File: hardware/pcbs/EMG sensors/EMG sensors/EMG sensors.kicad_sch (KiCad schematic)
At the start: 28 parts, among them IC1 INA128, J1 Conn_01x04_Pin, J2 Conn_01x01_Pin, U6 OPA2188AIDR, U7 OPA188AIDR

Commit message: sEMG sensors v0.3
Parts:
- added R11: 1M, Resistor_SMD:R_0603_1608Metric_Pad0.98x0.95mm_HandSolder, symbol Device:R
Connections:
- net GND: now also R11.1; no longer J2.1 (Pin_1)
- new net Ref: J2.1 (Pin_1), R11.2
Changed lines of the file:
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@@
-	(wire
-		(pts
-			(xy 57.658 144.78) (xy 57.658 146.812)
-		)
-		(stroke
-			(width 0)
-			(type default)
-		)
-	)
 	(wire
 		(pts
@@
 	(wire
 		(pts
+			(xy 57.658 144.78) (xy 57.658 147.574)
+		)
+		(stroke
+			(width 0)
+			(type default)
+		)
+	)
+	(wire
+		(pts
 			(xy 249.936 84.582) (xy 250.19 84.582)
 		)
@@
 	(wire
 		(pts
+			(xy 57.658 155.194) (xy 57.658 156.21)
+		)
+		(stroke
+			(width 0)
+			(type default)
+		)
+	)
+	(wire
+		(pts
 			(xy 202.692 84.582) (xy 212.344 84.582)
 		)
@@
 	(global_label "Ref"
 		(shape input)
-		(at 57.658 146.812 270)
+		(at 57.658 156.21 270)
 		(fields_autoplaced yes)
 		(effects
@@
 		)
 		(property "Intersheetrefs" "${INTERSHEET_REFS}"
-			(at 57.658 152.8815 90)
+			(at 57.658 162.2795 90)
 			(effects
 				(font
@@
 					(unit 1)
 				)
+			)
+		)
+	)
+	(symbol
+		(lib_id "Device:R")
+		(at 57.658 151.384 0)
+		(unit 1)
+		(exclude_from_sim no)
+		(in_bom yes)
+		(on_board yes)
+		(dnp no)
+		(fields_autoplaced yes)
+		(property "Reference" "R11"
+			(at 59.69 150.1139 0)
+			(effects
+				(font
+					(size 1.27 1.27)
+				)
+				(justify left)
+			)
+		)
+		(property "Value" "1M"
+			(at 59.69 152.6539 0)
+			(effects
+				(font
+					(size 1.27 1.27)
+				)
+				(justify left)
+			)
+		)
+		(property "Footprint" "Resistor_SMD:R_0603_1608Metric_Pad0.98x0.95mm_HandSolder"
+			(at 55.88 151.384 90)
+			(effects
+				(font
+					(size 1.27 1.27)
+				)
+				(hide yes)
+			)
+		)
+		(property "Datasheet" "~"
+			(at 57.658 151.384 0)
+			(effects
+				(font
+					(size 1.27 1.27)
+				)
+				(hide yes)
+			)
+		)
+		(property "Description" "Resistor"
+			(at 57.658 151.384 0)
+			(effects
+				(font
+					(size 1.27 1.27)
+				)
+				(hide yes)
+			)
+		)
+		(pin "1"
+		)
+		(pin "2"
+		)
+		(instances
+			(project ""
+				(path "/a1d73765-1778-424a-b5d5-45dcc9997ebd"
+					(reference "R11")
+					(unit 1)
+				)

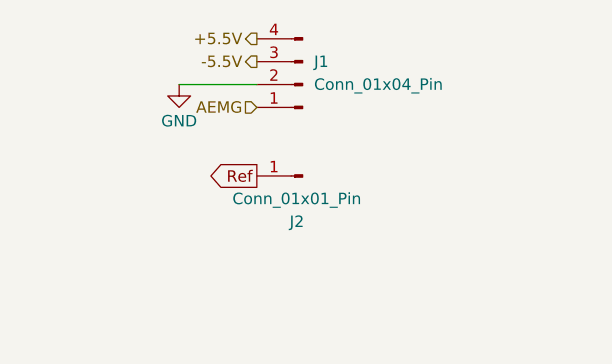
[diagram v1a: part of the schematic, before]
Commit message: Connector update of the sEMG sensor
Changed it to be JST_GH_SM04B instead of JST_GH_BM04B for easier use
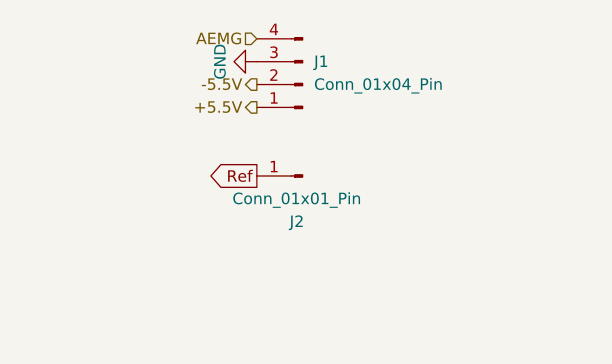
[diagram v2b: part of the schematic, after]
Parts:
- J1: footprint Connector_JST:JST_GH_BM04B-GHS-TBT_1x04-1MP_P1.25mm_Vertical -> Connector_JST:JST_GH_SM04B-GHS-TB_1x04-1MP_P1.25mm_Horizontal
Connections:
- net +5.5V: now also J1.1 (Pin_1); no longer J1.4 (Pin_4)
- net -5.5V: now also J1.2 (Pin_2); no longer J1.3 (Pin_3)
- net AEMG: now also J1.4 (Pin_4); no longer J1.1 (Pin_1)
- net GND: now also J1.3 (Pin_3); no longer J1.2 (Pin_2)
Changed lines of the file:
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@@
-	(wire
-		(pts
-			(xy 54.61 29.21) (xy 63.246 29.21)
-		)
-		(stroke
-			(width 0)
-			(type default)
-		)
-	)
 	(wire
 		(pts
@@
 	(hierarchical_label "-5.5V"
 		(shape output)
-		(at 63.246 26.67 180)
+		(at 63.246 29.21 180)
 		(effects
 			(font
@@
 	(hierarchical_label "AEMG"
 		(shape input)
-		(at 63.246 31.75 180)
+		(at 63.246 24.13 180)
 		(effects
 			(font
@@
 	(hierarchical_label "+5.5V"
 		(shape output)
-		(at 63.246 24.13 180)
+		(at 63.246 31.75 180)
 		(effects
 			(font
@@
 	(symbol
 		(lib_id "power:GND")
-		(at 54.61 29.21 0)
+		(at 63.246 26.67 270)
 		(unit 1)
 		(exclude_from_sim no)
@@
 		(dnp no)
 		(property "Reference" "#PWR04"
-			(at 54.61 35.56 0)
+			(at 56.896 26.67 0)
 			(effects
 				(font
@@
 		)
 		(property "Value" "GND"
-			(at 54.61 33.274 0)
+			(at 59.182 26.67 0)
 			(effects
 				(font
@@
 		)
 		(property "Footprint" ""
-			(at 54.61 29.21 0)
+			(at 63.246 26.67 0)
 			(effects
 				(font
@@
 		)
 		(property "Datasheet" ""
-			(at 54.61 29.21 0)
+			(at 63.246 26.67 0)
 			(effects
 				(font
@@
 		)
 		(property "Description" "Power symbol creates a global label with name \"GND\" , ground"
-			(at 54.61 29.21 0)
+			(at 63.246 26.67 0)
 			(effects
 				(font
@@
 			)
 		)
-		(property "Footprint" "Connector_JST:JST_GH_BM04B-GHS-TBT_1x04-1MP_P1.25mm_Vertical"
+		(property "Footprint" "Connector_JST:JST_GH_SM04B-GHS-TB_1x04-1MP_P1.25mm_Horizontal"
 			(at 68.326 29.21 0)
 			(effects

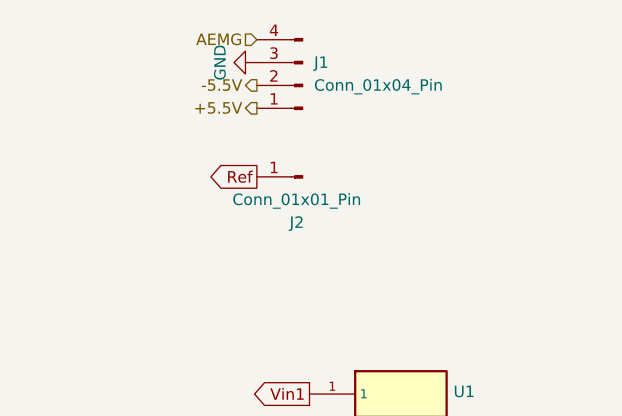
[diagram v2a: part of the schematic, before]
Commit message: ADC + sEMG changes
sEMG - connector updates
ADC - major changes - connectors, layout changes
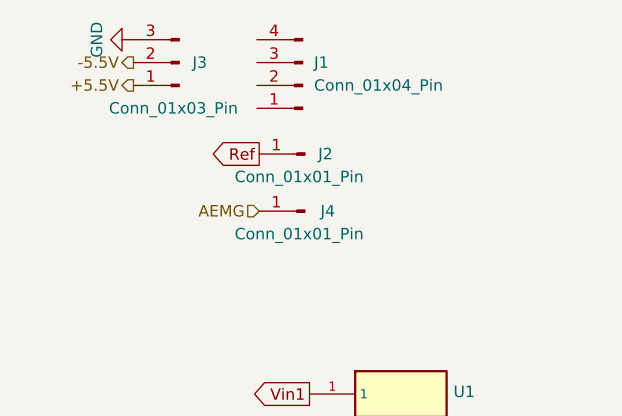
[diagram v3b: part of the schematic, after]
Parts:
- added J3: Conn_01x03_Pin, Connector_JST:JST_GH_SM03B-GHS-TB_1x03-1MP_P1.25mm_Horizontal, symbol Connector:Conn_01x03_Pin
- added J4: Conn_01x01_Pin, Connectors:DIN_Male_1PIN_1.5mm, symbol Connector:Conn_01x01_Pin
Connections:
- net +5.5V: now also J3.1 (Pin_1); no longer J1.1 (Pin_1)
- net -5.5V: now also J3.2 (Pin_2); no longer J1.2 (Pin_2)
- net AEMG: now also J4.1 (Pin_1); no longer J1.4 (Pin_4)
- net GND: now also J3.3 (Pin_3); no longer J1.3 (Pin_3)
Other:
- moved on the sheet: J2
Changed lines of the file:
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@@
 	(global_label "Ref"
 		(shape output)
-		(at 63.246 39.37 180)
+		(at 63.5 36.83 180)
 		(fields_autoplaced yes)
 		(effects
@@
 		)
 		(property "Intersheetrefs" "${INTERSHEET_REFS}"
-			(at 57.1765 39.37 0)
+			(at 57.4305 36.83 0)
 			(effects
 				(font
@@
 		)
 	)
-	(hierarchical_label "-5.5V"
+	(hierarchical_label "+5.5V"
 		(shape output)
-		(at 63.246 29.21 180)
+		(at 49.53 29.21 180)
 		(effects
 			(font
@@
 	(hierarchical_label "AEMG"
 		(shape input)
-		(at 63.246 24.13 180)
+		(at 63.5 43.18 180)
 		(effects
 			(font
@@
 		)
 	)
-	(hierarchical_label "+5.5V"
+	(hierarchical_label "-5.5V"
 		(shape output)
-		(at 63.246 31.75 180)
+		(at 49.53 26.67 180)
 		(effects
 			(font
@@
 	(symbol
 		(lib_id "power:GND")
-		(at 63.246 26.67 270)
+		(at 49.53 24.13 270)
 		(unit 1)
 		(exclude_from_sim no)
@@
 		(dnp no)
 		(property "Reference" "#PWR04"
-			(at 56.896 26.67 0)
+			(at 43.18 24.13 0)
 			(effects
 				(font
@@
 		)
 		(property "Value" "GND"
-			(at 59.182 26.67 0)
+			(at 45.466 24.13 0)
 			(effects
 				(font
@@
 		)
 		(property "Footprint" ""
-			(at 63.246 26.67 0)
+			(at 49.53 24.13 0)
 			(effects
 				(font
@@
 		)
 		(property "Datasheet" ""
-			(at 63.246 26.67 0)
+			(at 49.53 24.13 0)
 			(effects
 				(font
@@
 		)
 		(property "Description" "Power symbol creates a global label with name \"GND\" , ground"
-			(at 63.246 26.67 0)
+			(at 49.53 24.13 0)
 			(effects
 				(font
@@
 	)
 	(symbol
+		(lib_id "Connector:Conn_01x01_Pin")
+		(at 68.58 43.18 180)
+		(unit 1)
+		(exclude_from_sim no)
+		(in_bom yes)
+		(on_board yes)
+		(dnp no)
+		(property "Reference" "J4"
+			(at 71.12 43.18 0)
+			(effects
+				(font
+					(size 1.27 1.27)
+				)
+			)
+		)
+		(property "Value" "Conn_01x01_Pin"
+			(at 67.945 45.72 0)
+			(effects
+				(font
+					(size 1.27 1.27)
+				)
+			)
+		)
+		(property "Footprint" "Connectors:DIN_Male_1PIN_1.5mm"
+			(at 68.58 43.18 0)
+			(effects
+				(font
+					(size 1.27 1.27)
+				)
+				(hide yes)
+			)
+		)
+		(property "Datasheet" "~"
+			(at 68.58 43.18 0)
+			(effects
+				(font
+					(size 1.27 1.27)
+				)
+				(hide yes)
+			)
+		)
+		(property "Description" "Generic connector, single row, 01x01, script generated"
+			(at 68.58 43.18 0)
+			(effects
+				(font
+					(size 1.27 1.27)
+				)
+				(hide yes)
+			)
+		)
+		(pin "1"
+		)
+		(instances
+			(project "EMG sensors"
+				(path "/a1d73765-1778-424a-b5d5-45dcc9997ebd"
+					(reference "J4")
+					(unit 1)
+				)
+			)
+		)
+	)
+	(symbol
 		(lib_id "headers:H_1")
 		(at 62.738 69.85 0)
@@
 	(symbol
 		(lib_id "Connector:Conn_01x01_Pin")
-		(at 68.326 39.37 180)
+		(at 68.58 36.83 180)
 		(unit 1)
 		(exclude_from_sim no)
@@
 		(dnp no)
 		(property "Reference" "J2"
-			(at 67.691 44.45 0)
+			(at 70.866 36.83 0)
 			(effects
 				(font
@@
 		)
 		(property "Value" "Conn_01x01_Pin"
-			(at 67.691 41.91 0)
+			(at 67.945 39.37 0)
 			(effects
 				(font
@@
 		)
 		(property "Footprint" "Connectors:DIN_Male_1PIN_1.5mm"
-			(at 68.326 39.37 0)
+			(at 68.58 36.83 0)
 			(effects
 				(font
@@
 		)
 		(property "Datasheet" "~"
-			(at 68.326 39.37 0)
+			(at 68.58 36.83 0)
 			(effects
 				(font
@@
 		)
 		(property "Description" "Generic connector, single row, 01x01, script generated"
-			(at 68.326 39.37 0)
+			(at 68.58 36.83 0)
 			(effects
 				(font
@@
 					(unit 1)
 				)
+			)
+		)
+	)
+	(symbol
+		(lib_id "Connector:Conn_01x03_Pin")
+		(at 54.61 26.67 180)
+		(unit 1)
+		(exclude_from_sim no)
+		(in_bom yes)
+		(on_board yes)
+		(dnp no)
+		(property "Reference" "J3"
+			(at 56.896 26.67 0)
+			(effects
+				(font
+					(size 1.27 1.27)
+				)
+			)
+		)
+		(property "Value" "Conn_01x03_Pin"
+			(at 53.975 31.75 0)
+			(effects
+				(font
+					(size 1.27 1.27)
+				)
+			)
+		)
+		(property "Footprint" "Connector_JST:JST_GH_SM03B-GHS-TB_1x03-1MP_P1.25mm_Horizontal"
+			(at 54.61 26.67 0)
+			(effects
+				(font
+					(size 1.27 1.27)
+				)
+				(hide yes)
+			)
+		)
+		(property "Datasheet" "~"
+			(at 54.61 26.67 0)
+			(effects
+				(font
+					(size 1.27 1.27)
+				)
+				(hide yes)
+			)
+		)
+		(property "Description" "Generic connector, single row, 01x03, script generated"
+			(at 54.61 26.67 0)
+			(effects
+				(font
+					(size 1.27 1.27)
+				)
+				(hide yes)
+			)
+		)
+		(pin "3"
+		)
+		(pin "1"
+		)
+		(pin "2"
+		)
+		(instances
+			(project ""
+				(path "/a1d73765-1778-424a-b5d5-45dcc9997ebd"
+					(reference "J3")
+					(unit 1)
+				)

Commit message: BMS v0.3 + main folder reconstruction
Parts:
- removed J1: Conn_01x04_Pin, Connector_JST:JST_GH_SM04B-GHS-TB_1x04-1MP_P1.25mm_Horizontal, symbol Connector:Conn_01x04_Pin
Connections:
- net Ref: no longer names the net of J2.1 (Pin_1), R11.2
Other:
- moved on the sheet: J2, J4, R11
